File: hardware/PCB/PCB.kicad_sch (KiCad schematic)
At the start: 14 parts, among them J1 Header, J2 Conn_01x02, J3 Conn_01x01_Male, U1 GAL16V8, U2 74LVC245A, U3 74LVC245A

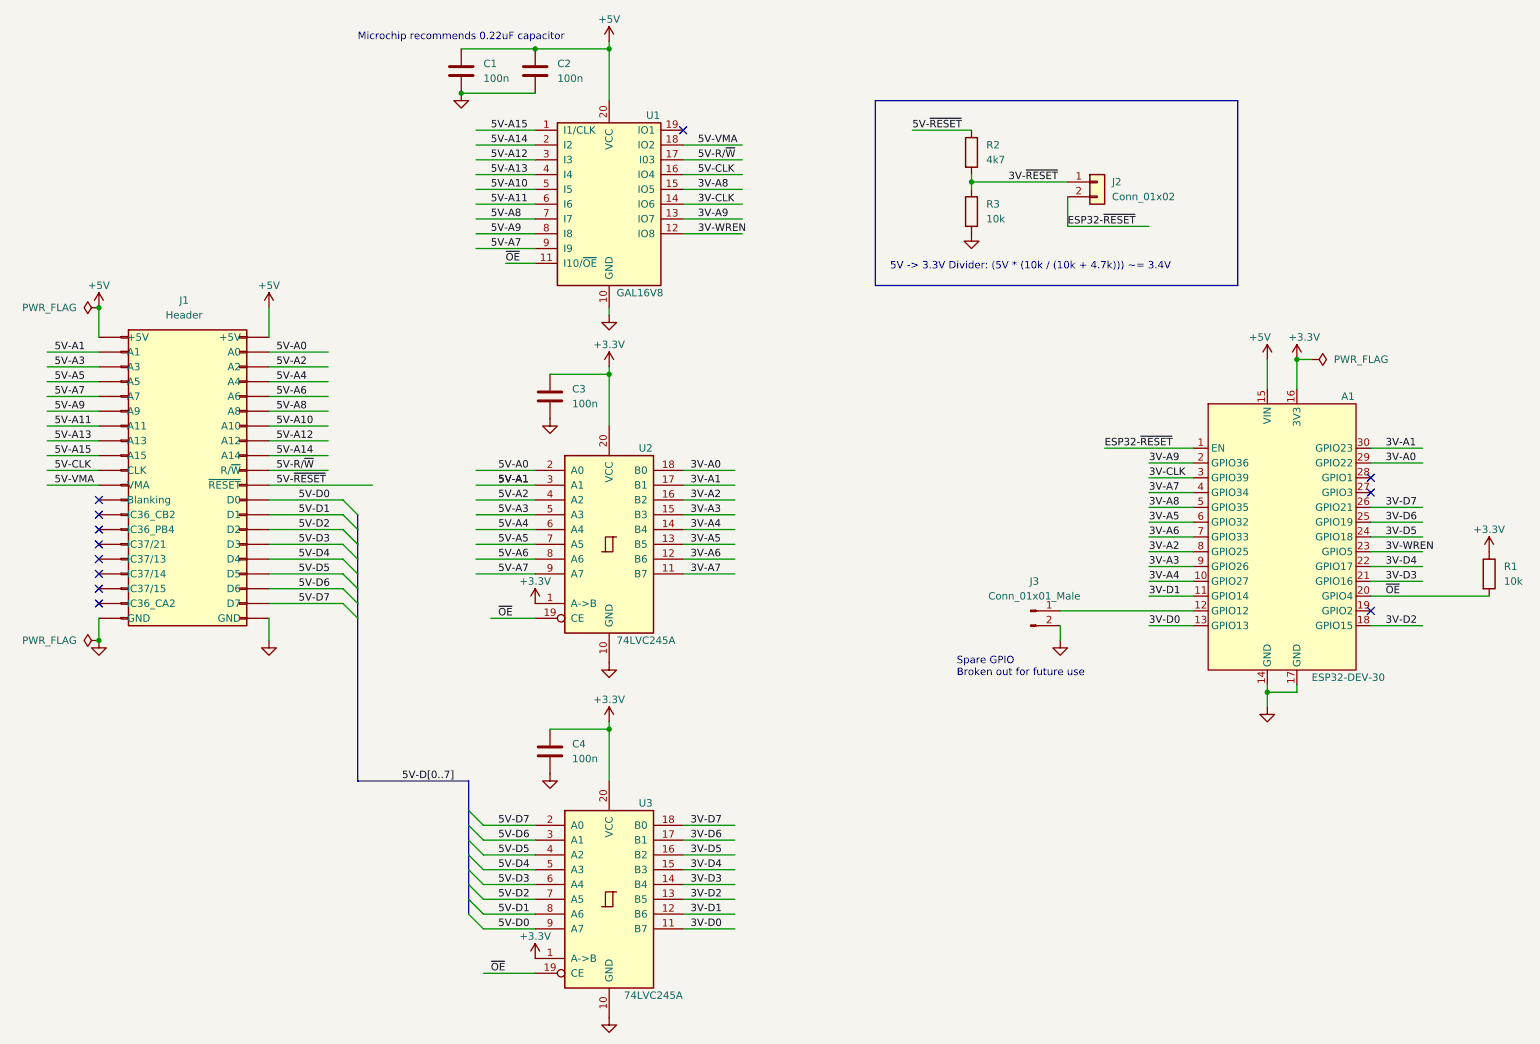
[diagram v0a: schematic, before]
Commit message: pcb: create rev2, using raspberry pi pico w
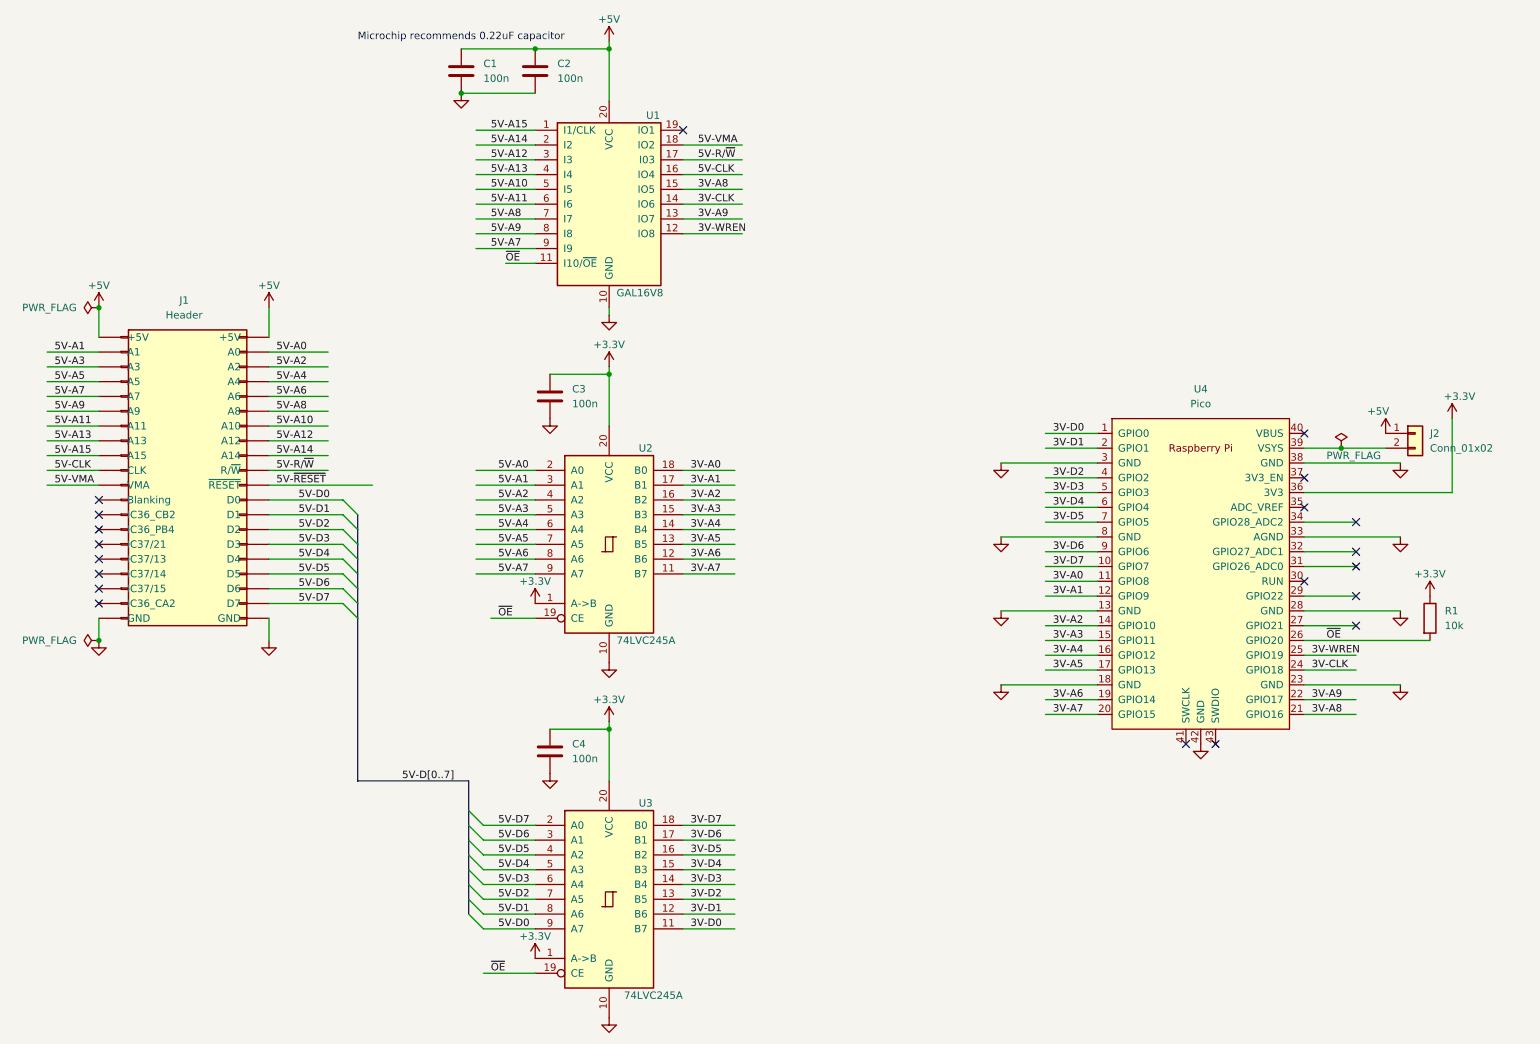
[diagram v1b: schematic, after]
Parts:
- removed A1: ESP32-DEV-30, footprint-library:esp32_devkit_v1_doit, symbol symbol-library:ESP32-DEV-30
- removed J3: Conn_01x01_Male, Connector_PinHeader_2.54mm:PinHeader_1x02_P2.54mm_Vertical, symbol Connector:Conn_01x02_Male
- removed R2: 4k7, Resistor_THT:R_Axial_DIN0207_L6.3mm_D2.5mm_P10.16mm_Horizontal, symbol Device:R
- removed R3: 10k, Resistor_THT:R_Axial_DIN0207_L6.3mm_D2.5mm_P10.16mm_Horizontal, symbol Device:R
- added U4: Pico, MCU_RaspberryPi_and_Boards:RPi_PicoW_SMD_TH, symbol MCU_RaspberryPi_and_Boards:Pico
- C1, C2, C3, C4: footprint Capacitor_THT:C_Disc_D7.0mm_W2.5mm_P5.00mm -> Capacitor_THT:C_Disc_D3.4mm_W2.1mm_P2.50mm
- J2: footprint Connector_PinHeader_2.54mm:PinHeader_1x02_P2.54mm_Vertical -> (none)
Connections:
- net 3V-~{RESET} is gone; now on net +5V: J2.1 (Pin_1)
- net +3.3V: now also U4.36 (3V3)
- net 3V-A0: now also U4.11 (GPIO8)
- net 3V-A1: now also U4.12 (GPIO9)
- net 3V-A2: now also U4.14 (GPIO10)
- net 3V-A3: now also U4.15 (GPIO11)
- net 3V-A4: now also U4.16 (GPIO12)
- net 3V-A5: now also U4.17 (GPIO13)
- net 3V-A6: now also U4.19 (GPIO14)
- net 3V-A7: now also U4.20 (GPIO15)
- net 3V-A8: now also U4.21 (GPIO16)
- net 3V-A9: now also U4.22 (GPIO17)
- net 3V-CLK: now also U4.24 (GPIO18)
- net 3V-D0: now also U4.1 (GPIO0)
- net 3V-D1: now also U4.2 (GPIO1)
- net 3V-D2: now also U4.4 (GPIO2)
- net 3V-D3: now also U4.5 (GPIO3)
- net 3V-D4: now also U4.6 (GPIO4)
- net 3V-D5: now also U4.7 (GPIO5)
- net 3V-D6: now also U4.9 (GPIO6)
- net 3V-D7: now also U4.10 (GPIO7)
- net 3V-WREN: now also U4.25 (GPIO19)
- net GND: now also U4.13 (GND), U4.18 (GND), U4.23 (GND), U4.28 (GND), U4.3 (GND), U4.33 (AGND), U4.38 (GND), U4.42 (GND), U4.8 (GND)
- net ~{OE}: now also U4.26 (GPIO20)
- net ESP32-~{RESET}: no longer names the net of J2.2 (Pin_2)
- net ESP32-~{RESET}: now also U4.39 (VSYS)
- no-connect marks 12 -> 20
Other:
- note removed: "5V -> 3.3V Divider: (5V * (10k / (10k + 4.7k))) ~= 3.4V"
- note removed: "Spare GPIO Broken out for future use"
- moved on the sheet: R1

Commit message: Finish PCB rev2
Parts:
- removed J2: Conn_01x02, symbol Connector_Generic:Conn_01x02
- added D1: 1N5819, Diode_THT:D_DO-41_SOD81_P10.16mm_Horizontal, symbol Diode:1N5819
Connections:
- net +5V: now also D1.2 (A)
- net at U4.39 (VSYS): now also D1.1 (K)
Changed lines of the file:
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@@
     (pin "1")
+  )
+  (symbol (lib_id "Diode:1N5819") (at 247.65 86.36 90) (unit 1)
+    (in_bom yes) (on_board yes)
+    (property "Reference" "D1" (id 0) (at 250.19 86.36 90)
+      (effects (font (size 1.27 1.27)) (justify right))
+    )
+    (property "Value" "1N5819" (id 1) (at 248.92 88.9 90)
+      (effects (font (size 1.27 1.27)) (justify right))
+    )
+    (property "Footprint" "Diode_THT:D_DO-41_SOD81_P10.16mm_Horizontal" (id 2) (at 252.095 86.36 0)
+      (effects (font (size 1.27 1.27)) hide)
+    )
+    (property "Datasheet" "http://www.vishay.com/docs/88525/1n5817.pdf" (id 3) (at 247.65 86.36 0)
+      (effects (font (size 1.27 1.27)) hide)
+    )
+    (pin "1")
+    (pin "2")
   )
   (symbol (lib_id "power:GND") (at 250.19 105.41 0) (mirror y) (unit 1)
@@
     )
     (pin "1")
-  )
-  (symbol (lib_id "Connector_Generic:Conn_01x02") (at 252.73 87.63 0) (unit 1)
-    (in_bom yes) (on_board yes) (fields_autoplaced)
-    (property "Reference" "J2" (id 0) (at 255.27 87.6299 0)
-      (effects (font (size 1.27 1.27)) (justify left))
-    )
-    (property "Value" "Conn_01x02" (id 1) (at 255.27 90.1699 0)
-      (effects (font (size 1.27 1.27)) (justify left))
-    )
-    (property "Footprint" "" (id 2) (at 252.73 87.63 0)
-      (effects (font (size 1.27 1.27)) hide)
-    )
-    (property "Datasheet" "~" (id 3) (at 252.73 87.63 0)
-      (effects (font (size 1.27 1.27)) hide)
-    )
-    (pin "1")
-    (pin "2")
   )
   (symbol (lib_id "power:PWR_FLAG") (at 26.67 123.19 90) (unit 1)
@@
     (pin "1")
   )
-  (symbol (lib_id "power:+5V") (at 247.65 87.63 0) (unit 1)
-    (in_bom yes) (on_board yes)
-    (property "Reference" "#PWR021" (id 0) (at 247.65 91.44 0)
-      (effects (font (size 1.27 1.27)) hide)
-    )
-    (property "Value" "+5V" (id 1) (at 246.38 83.82 0))
-    (property "Footprint" "" (id 2) (at 247.65 87.63 0)
-      (effects (font (size 1.27 1.27)) hide)
-    )
-    (property "Datasheet" "" (id 3) (at 247.65 87.63 0)
+  (symbol (lib_id "power:+5V") (at 247.65 82.55 0) (unit 1)
+    (in_bom yes) (on_board yes)
+    (property "Reference" "#PWR021" (id 0) (at 247.65 86.36 0)
+      (effects (font (size 1.27 1.27)) hide)
+    )
+    (property "Value" "+5V" (id 1) (at 246.38 78.74 0))
+    (property "Footprint" "" (id 2) (at 247.65 82.55 0)
+      (effects (font (size 1.27 1.27)) hide)
+    )
+    (property "Datasheet" "" (id 3) (at 247.65 82.55 0)
       (effects (font (size 1.27 1.27)) hide)
     )
@@
       (reference "C4") (unit 1) (value "100n") (footprint "Capacitor_THT:C_Disc_D3.4mm_W2.1mm_P2.50mm")
     )
+    (path "/226e6c98-1fa1-49cc-8480-6e81e3a2b457"
+      (reference "D1") (unit 1) (value "1N5819") (footprint "Diode_THT:D_DO-41_SOD81_P10.16mm_Horizontal")
+    )
     (path "/13b76529-ca7c-4b05-b7e4-54b4f47a9856"
       (reference "J1") (unit 1) (value "Header") (footprint "Connector_PinSocket_2.54mm:PinSocket_2x20_P2.54mm_Vertical")
     )
-    (path "/59e69647-32a3-46bd-a426-0559418ab9d0"
-      (reference "J2") (unit 1) (value "Conn_01x02") (footprint "Connector_PinHeader_2.54mm:PinHeader_1x02_P2.54mm_Vertical")
-    )
     (path "/fcda4cd7-1f79-44e1-82ea-5eb3d23f02ed"
